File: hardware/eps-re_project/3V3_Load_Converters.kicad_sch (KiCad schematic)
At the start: 73 parts, among them Q10 EPC2016C, Q11 EPC2016C, Q12 EPC2016C, Q7 SI2302, Q8 SI2302, Q9 EPC2016C, U22 INA199C3DCKR

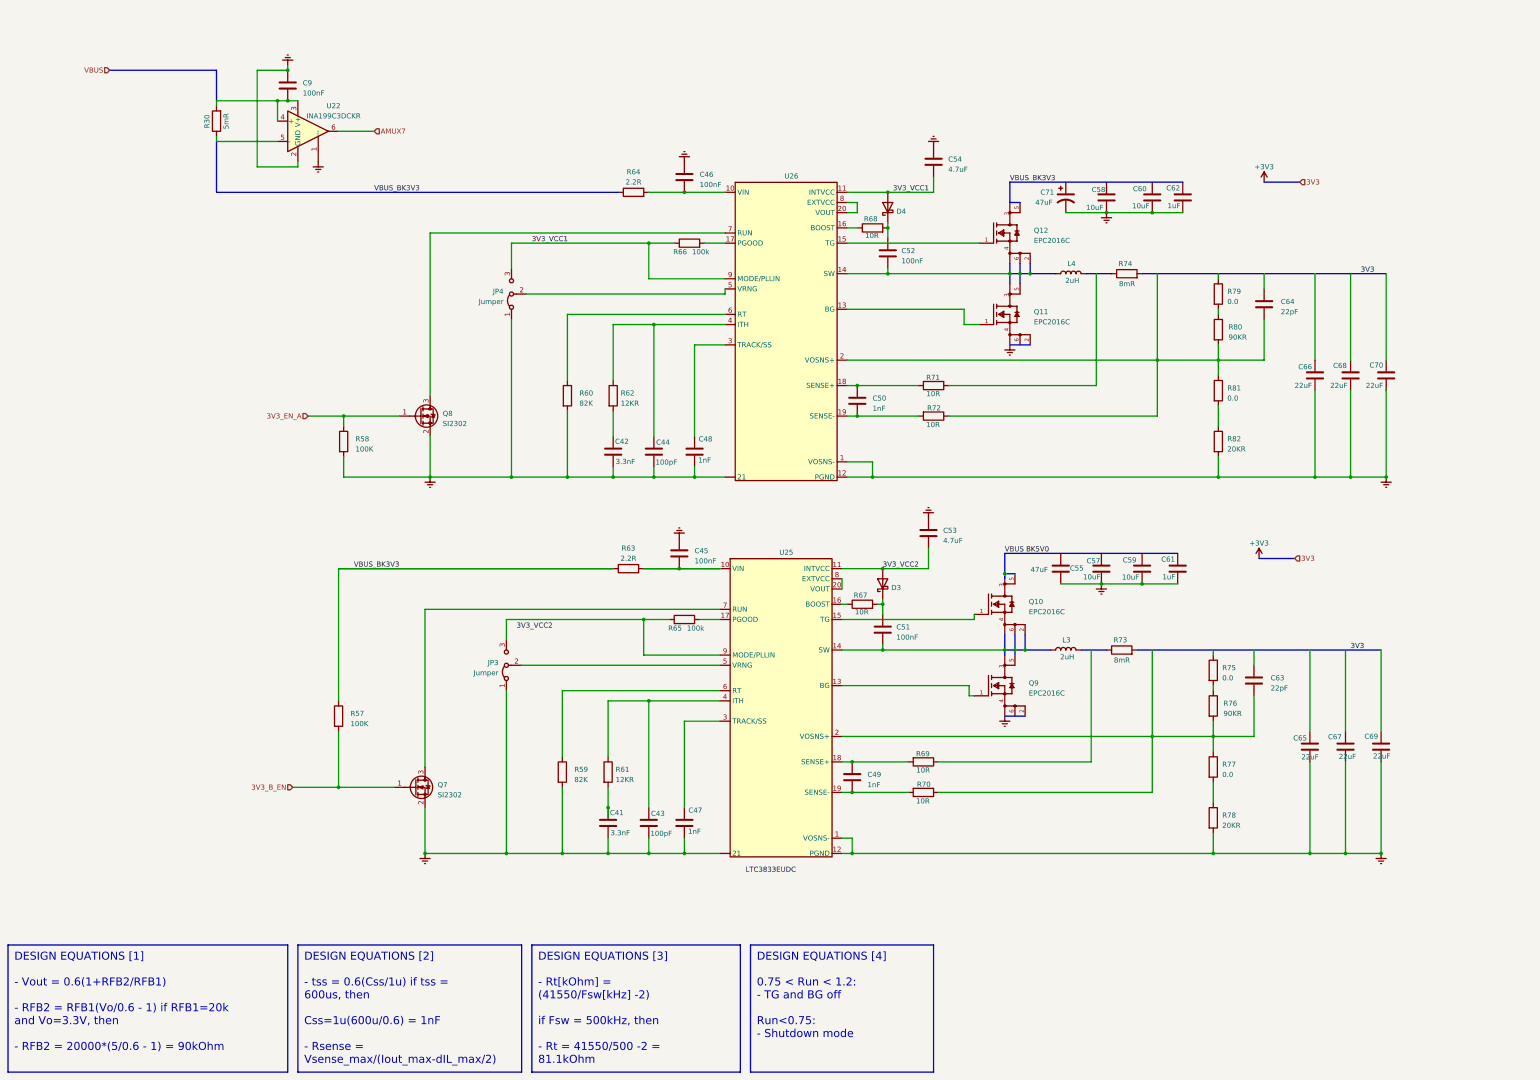
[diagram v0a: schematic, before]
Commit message: hardware: Restructuring the circuit, modifying symbols, footprints and other corrections
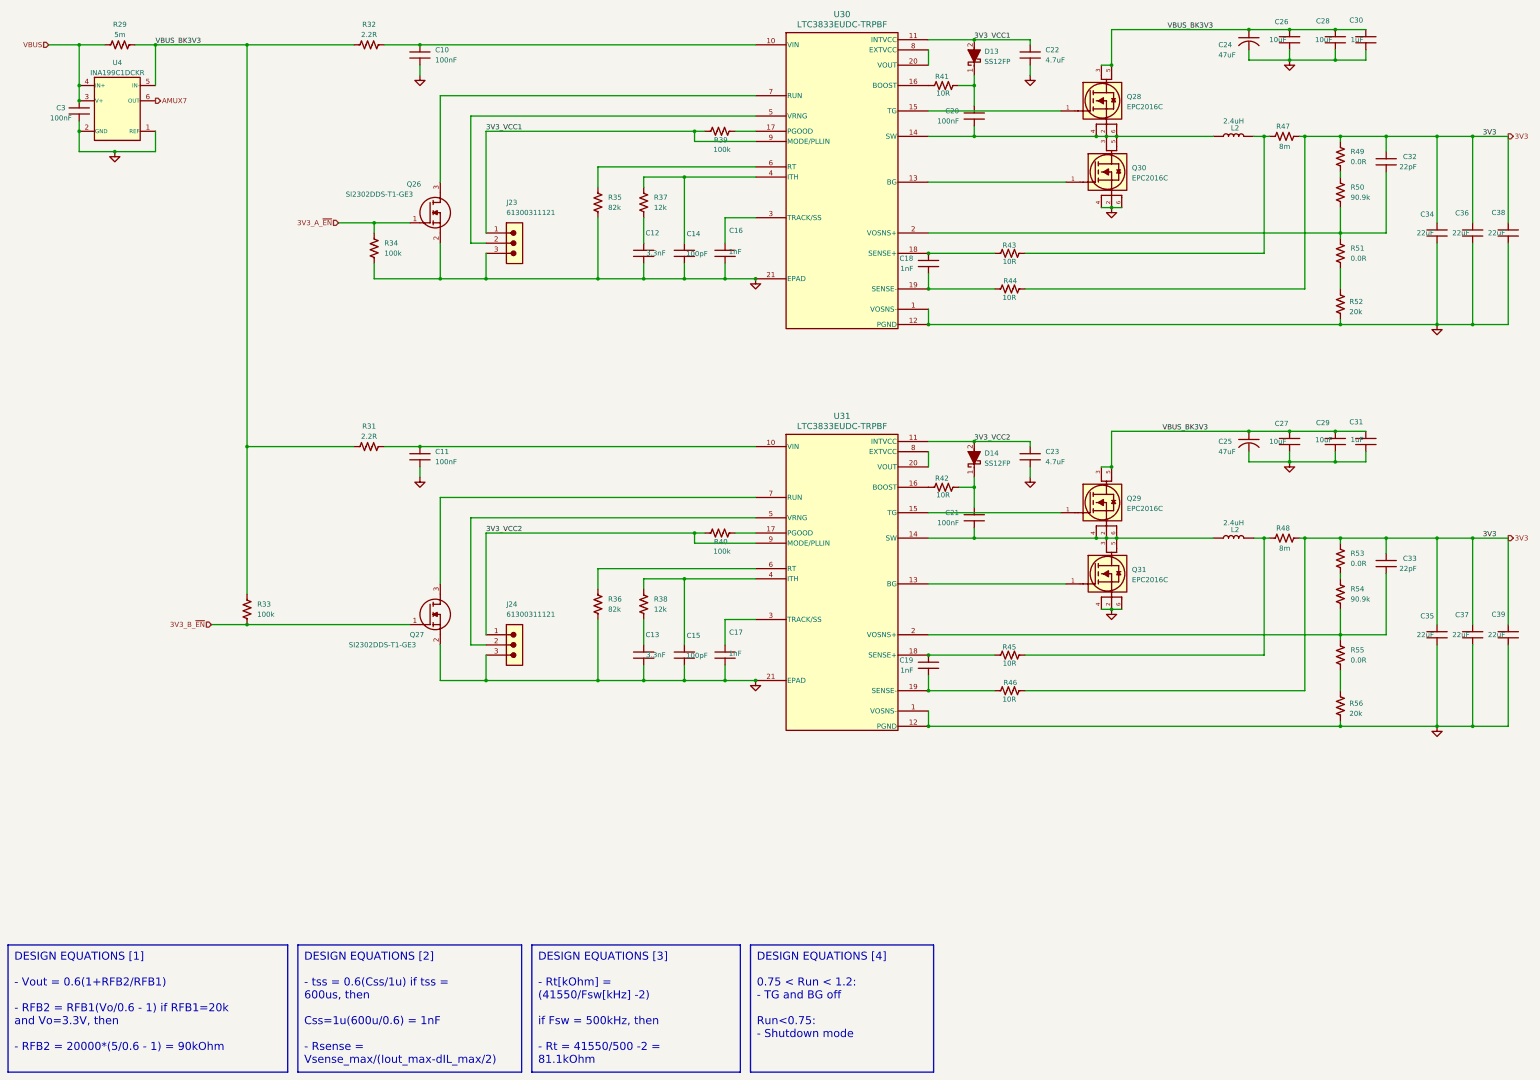
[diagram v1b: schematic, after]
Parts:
- removed C41, C42: 3.3nF, symbol Device:C
- removed C43, C44: 100pF, symbol Device:C
- removed C45, C46, C51, C52, C9: 100nF, symbol Device:C
- removed C47, C48, C49, C50: 1nF, symbol Device:C
- removed C53, C54: 4.7uF, symbol Device:C
- removed C55: 47uF, symbol Device:C
- removed C57, C58, C59, C60: 10uF, symbol Device:C
- removed C61, C62: 1uF, symbol Device:C
- removed C63, C64: 22pF, symbol Device:C
- removed C65, C66, C67, C68, C69, C70: 22uF, symbol Device:C
- removed C71: 47uF, symbol Device:C_Polarized_US
- removed D3, D4: ~, symbol Device:D_Schottky
- removed JP3, JP4: Jumper, symbol Jumper:Jumper_3_Bridged12
- removed L3, L4: 2uH, symbol Device:L
- removed Q10, Q11, Q12, Q9: EPC2016C, EPC-EPC2016C-*, symbol eec:EPC2016C
- removed Q7, Q8: SI2302, symbol Device:Q_NMOS_GSD
- removed R30: 5mR, symbol Device:R
- removed R57, R58: 100K, symbol Device:R
- removed R59, R60: 82K, symbol Device:R
- removed R61, R62: 12KR, symbol Device:R
- removed R63, R64: 2.2R, symbol Device:R
- removed R65, R66: 100k, symbol Device:R
- removed R67, R68, R69, R70, R71, R72: 10R, symbol Device:R
- removed R73, R74: 8mR, symbol Device:R
- removed R75, R77, R79, R81: 0.0, symbol Device:R
- removed R76, R80: 90KR, symbol Device:R
- removed R78, R82: 20KR, symbol Device:R
- removed U22: INA199C3DCKR, Package_TO_SOT_SMD:SOT-363_SC-70-6, symbol Amplifier_Current:INA199xxDCK
- removed U25, U26: ~, symbol New_Library:LTC3833EUDC
- added C10, C11, C20, C21, C3: 100nF, footprints:C0603C104K5RACTU, symbol C0603C104K5RACTU:C0603C104K5RACTU
- added C12, C13: 3.3nF, footprints:C0603C332J5GACAUTO, symbol C0603C332J5GACAUTO:C0603C332J5GACAUTO
- added C14, C15: 100pF, footprints:C0603C101J5GACAUTO, symbol C0603C101J5GACAUTO:C0603C101J5GACAUTO
- added C16, C17, C18, C19: 1nF, footprints:C0603C102F3GACTU, symbol C0603C102F3GACTU:C0603C102F3GACTU
- added C22, C23: 4.7uF, footprints:GCM32ER71H475KA55L, symbol GCM32ER71H475KA55L:GCM32ER71H475KA55L
- added C24, C25: 47uF, footprints:T495X476K035ATE300, symbol T495X476K035ATE300:T495X476K035ATE300
- added C26, C27, C28, C29: 10uF, footprints:C1210C106K5RACTU, symbol C1210C106K5RACTU:C1210C106K5RACTU
- added C30, C31: 1uF, footprints:C0805C105K5RACTU, symbol C0805C105K5RACTU:C0805C105K5RACTU
- added C32, C33: 22pF, footprints:C0603C220K5RACAUTO, symbol C0603C220K5RACAUTO:C0603C220K5RACAUTO
- added C34, C35, C36, C37, C38, C39: 22uF, footprints:GCM32ER71C226KE19L, symbol GCM32ER71C226KE19L:GCM32ER71C226KE19L
- added D13, D14: SS12FP, footprints:SS12FP, symbol SS12FP:SS12FP
- added J23, J24: 61300311121, footprints:61300311121, symbol 61300311121:61300311121
- added L2 (x2): 2.4uH, footprints:744325240, symbol 744325240:744325240
- added Q26, Q27: SI2302DDS-T1-GE3, footprints:SI2302DDS-T1-GE3, symbol SI2302DDS-T1-GE3:SI2302DDS-T1-GE3
- added Q28, Q29, Q30, Q31: EPC2016C, footprints:EPC2016C, symbol EPC2016C:EPC2016C
- added R29: 5m, symbol Device:R_US
- added R31, R32: 2.2R, symbol Device:R_US
- added R33, R34, R39, R40: 100k, symbol Device:R_US
- added R35, R36: 82k, symbol Device:R_US
- added R37, R38: 12k, symbol Device:R_US
- added R41, R42, R43, R44, R45, R46: 10R, symbol Device:R_US
- added R47, R48: 8m, symbol Device:R_US
- added R49, R51, R53, R55: 0.0R, symbol Device:R_US
- added R50, R54: 90.9k, symbol Device:R_US
- added R52, R56: 20k, symbol Device:R_US
- added U30, U31: LTC3833EUDC-TRPBF, footprints:LTC3833EUDC#TRPBF, symbol LTC3833EUDC#TRPBF:LTC3833EUDC-TRPBF
- added U4: INA199C1DCKR, footprints:INA199C1DCKR, symbol INA199C1DCKR:INA199xxDCK
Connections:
- net 3V3: now also C32.1, C33.1, C34.2, C35.2, C36.2, C37.2, C38.2, C39.2, R44.1, R46.1, R47.2, R48.2, R49.1, R53.1
- net 3V3_VCC1: now also C22.1, D13.2 (A), J23.1, R39.1, U30.11 (INTVCC), U30.9 (MODE/PLLIN)
- net 3V3_VCC2: now also C23.1, D14.2 (A), J24.1, R40.1, U31.11 (INTVCC), U31.9 (MODE/PLLIN)
- net AMUX7: now also U4.6 (OUT)
- net VBUS: now also C3.1, R29.1, U4.3 (V+), U4.4 (IN+)
- net VBUS_BK3V3: now also C24.2 (ANODE), C25.2 (ANODE), C26.1, C27.1, C28.1, C29.1, C30.1, C31.1, Q28.3 (Drain), Q28.5 (Drain), Q29.3 (Drain), Q29.5 (Drain), R29.2, R31.1, R32.1, R33.1, U4.5 (IN-)
- new net: R41.1, U30.16 (BOOST)
- new net: C20.1, D13.1 (K), R41.2
- new net: L2.2, R43.1, R47.1
- new net: C32.2, R50.2, R51.1, U30.2 (VOSNS+)
- new net: C19.1, R45.2, U31.18 (SENSE+)
- new net: C19.2, R46.2, U31.19 (SENSE-)
- new net: C10.2, R32.2, U30.10 (VIN)
- new net: C18.1, R43.2, U30.18 (SENSE+)
- new net: C18.2, R44.2, U30.19 (SENSE-)
- new net: C33.2, R54.2, R55.1, U31.2 (VOSNS+)
- new net: R55.2, R56.1
- new net: C14.1, R37.1, U30.4 (ITH)
- new net: C12.1, R37.2
- new net: C21.1, D14.1 (K), R42.2
- new net: R53.2, R54.1
- new net: Q27.3 (D), U31.7 (RUN)
- new net: R42.1, U31.16 (BOOST)
- new net: C20.2, L2.1, Q28.2 (Substrate), Q28.4 (Source), Q28.6 (Source), Q30.3 (Drain), Q30.5 (Drain), U30.14 (SW)
- new net: Q31.1 (Gate), U31.13 (BG)
- new net: C21.2, L2.1, Q29.2 (Substrate), Q29.4 (Source), Q29.6 (Source), Q31.3 (Drain), Q31.5 (Drain), U31.14 (SW)
- new net: C11.2, R31.2, U31.10 (VIN)
- new net: Q29.1 (Gate), U31.15 (TG)
- new net: R40.2, U31.17 (PGOOD)
- new net: U31.20 (VOUT), U31.8 (EXTVCC)
- new net: C17.1, U31.3 (TRACK/SS)
- new net: C15.1, R38.1, U31.4 (ITH)
- new net: J24.2, U31.5 (VRNG)
- new net: R36.1, U31.6 (RT)
- new net: J23.2, U30.5 (VRNG)
- new net: Q30.1 (Gate), U30.13 (BG)
- new net: Q28.1 (Gate), U30.15 (TG)
- new net: R39.2, U30.17 (PGOOD)
- new net: U30.20 (VOUT), U30.8 (EXTVCC)
- new net: C16.1, U30.3 (TRACK/SS)
- new net: R35.1, U30.6 (RT)
- new net: Q26.3 (D), U30.7 (RUN)
- new net: L2.2, R45.1, R48.1
- new net: C13.1, R38.2
- new net: R49.2, R50.1
- new net: R51.2, R52.1
- new net 3V3_A_~{EN}: Q26.1 (G), R34.1
- new net 3V3_B_~{EN}: Q27.1 (G), R33.2
- new net GND: C10.1, C11.1, C12.2, C13.2, C14.2, C15.2, C16.2, C17.2, C22.2, C23.2, C24.1 (CATHODE), C25.1 (CATHODE), C26.2, C27.2, C28.2, C29.2, C3.2, C30.2, C31.2, C34.1, C35.1, C36.1, C37.1, C38.1, C39.1, J23.3, J24.3, Q26.2 (S), Q27.2 (S), Q30.2 (Substrate), Q30.4 (Source), Q30.6 (Source), Q31.2 (Substrate), Q31.4 (Source), Q31.6 (Source), R34.2, R35.2, R36.2, R52.2, R56.2, U30.1 (VOSNS-), U30.12 (PGND), U30.21 (EPAD), U31.1 (VOSNS-), U31.12 (PGND), U31.21 (EPAD), U4.1 (REF), U4.2 (GND)
